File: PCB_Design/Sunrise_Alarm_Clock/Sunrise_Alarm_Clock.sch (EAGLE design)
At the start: 25 parts, among them T1 2N3904, T2 2N3904, T3 2N3904, T4 2N3904

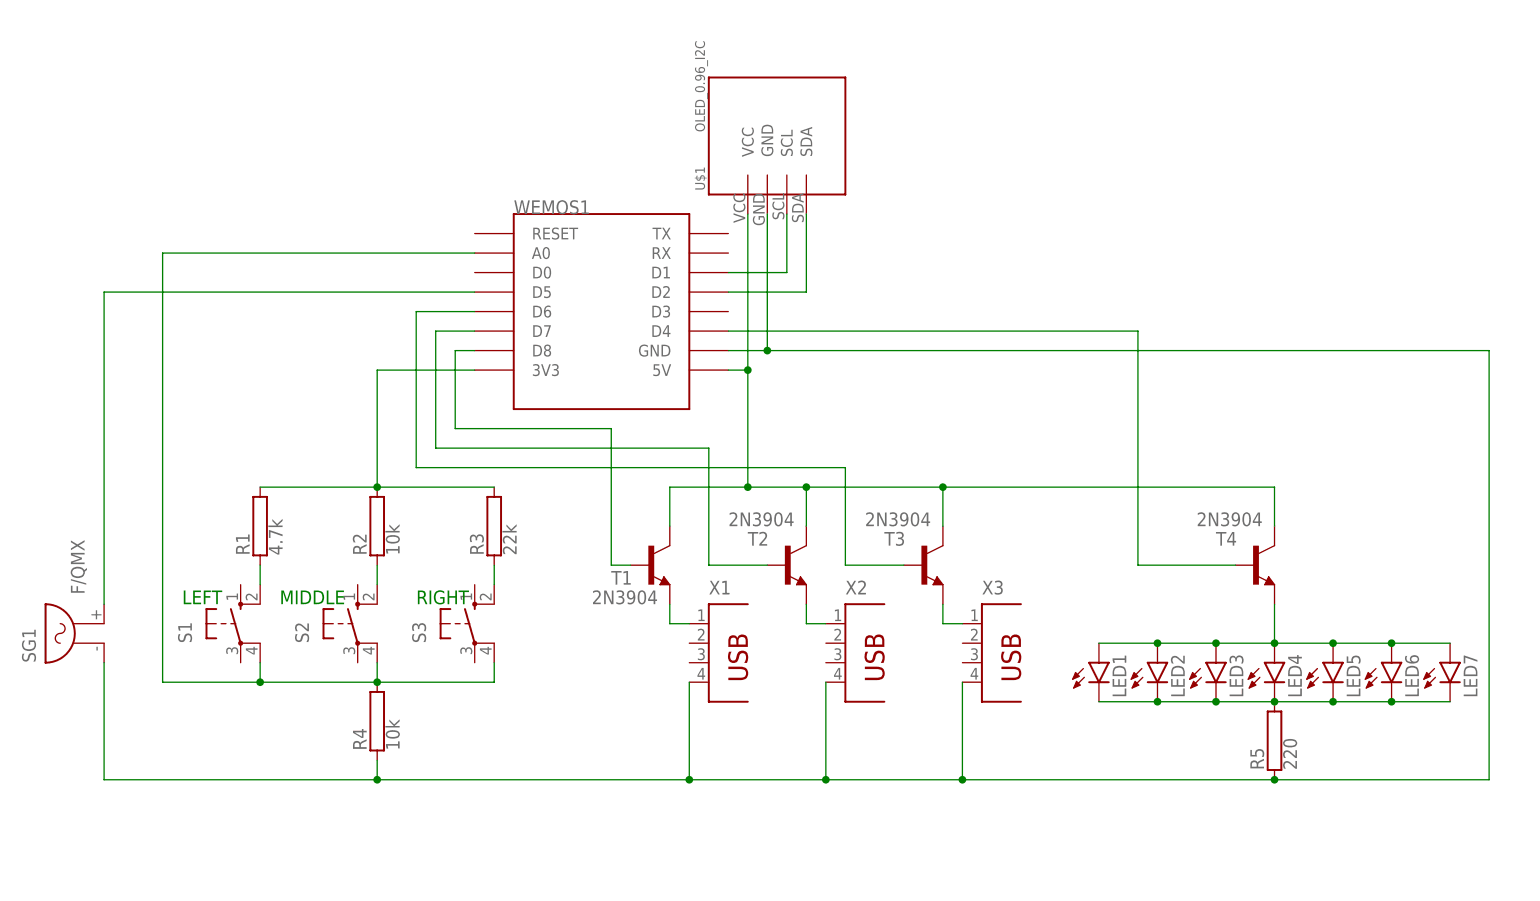
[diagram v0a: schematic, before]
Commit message: V2.1.1-alpha PCB V1.1
- Placed LEDs, USBs and D1 mini on the rear of the board
- Changed USB footprint to include shield pads
- Fixed transistors to be common-emitter
- Broke schematic into sections to make it easier to follow
- Hand-routed thicker traces
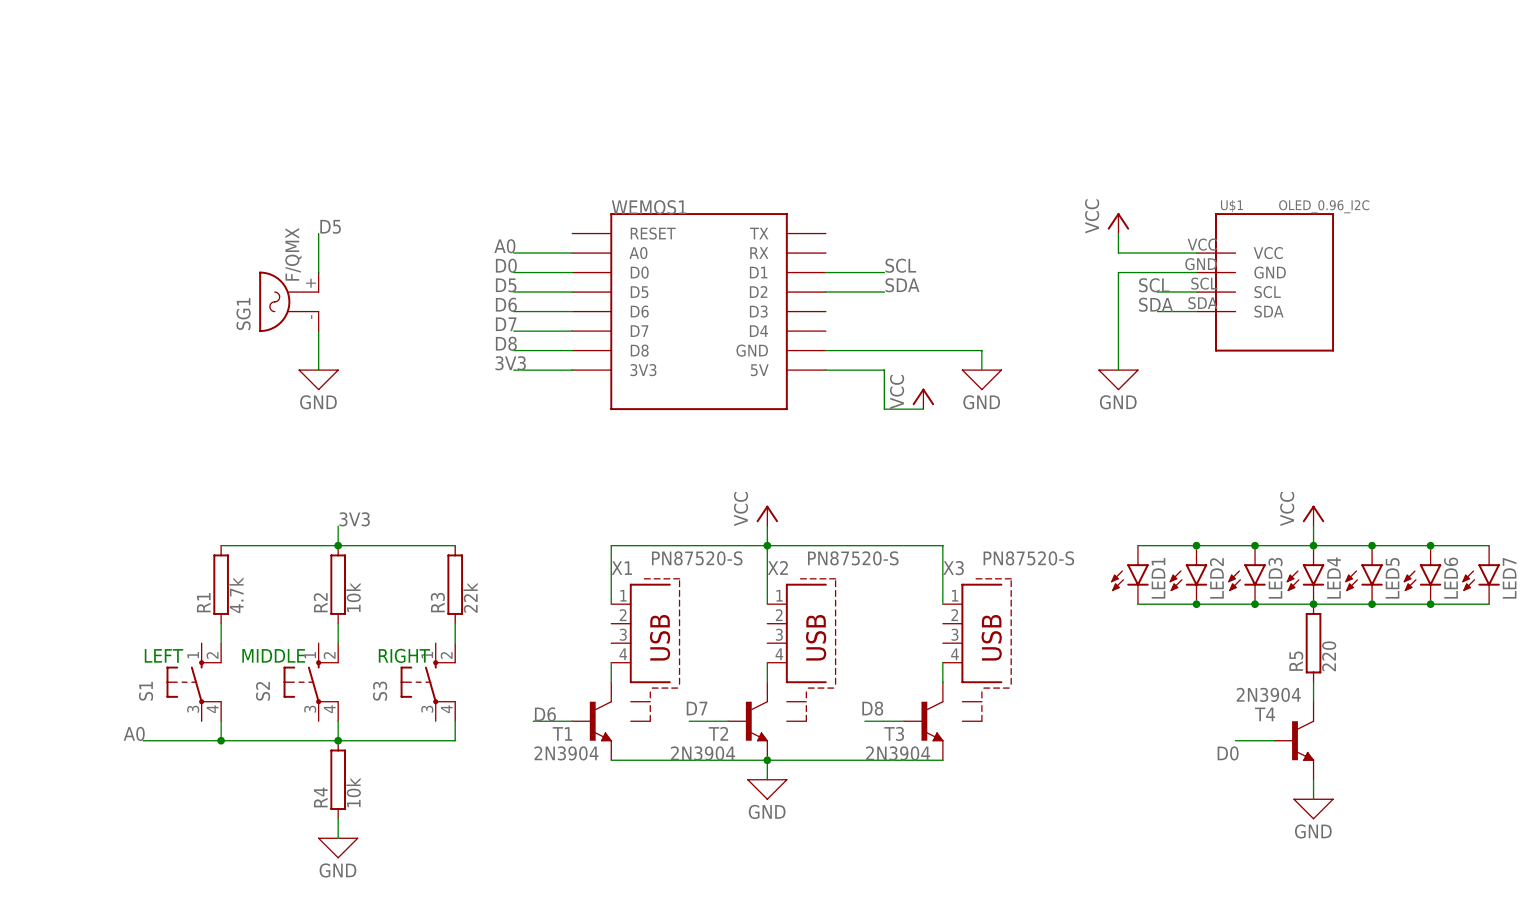
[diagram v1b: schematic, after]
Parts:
- X1, X2, X3: value (none) -> PN87520-S; device con-berg:PN87520 -> con-berg:PN87520-S
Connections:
- net N$10 renamed A0
- net N$12 renamed 3V3
- net N$15 renamed D5
- net N$17 renamed D7
- net N$3 renamed SCL
- net N$4 renamed SDA
- removed net N$13: T3.B, WEMOS1.D6
- removed net N$16: T1.B, WEMOS1.D8
- removed net N$19: LED1.A, LED2.A, LED3.A, LED4.A, LED5.A, LED6.A, LED7.A, T4.E
- removed net N$2: R4.1, R5.1, SG1.1, U$1.GND, WEMOS1.GND, X1.4, X2.4, X3.4
- removed net N$20: T4.B, WEMOS1.D4
- removed net N$7: T3.E, X3.1
- new net D0: T4.B, WEMOS1.D0
- new net D6: T1.B, WEMOS1.D6
- new net D8: T3.B, WEMOS1.D8
- new net GND: R4.1, SG1.1, T1.E, T2.E, T3.E, T4.E, U$1.GND, WEMOS1.GND
- new net N$14: R5.1, T4.C
- new net VCC: LED1.A, LED2.A, LED3.A, LED4.A, LED5.A, LED6.A, LED7.A, U$1.VCC, WEMOS1.5V, X1.1, X2.1, X3.1
- net N$1: now also X3.4; no longer T1.C, T2.C, T4.C, U$1.VCC, WEMOS1.5V
- net N$5: now also T2.C, X2.4; no longer T1.E, X1.1
- net N$6: now also T1.C, X1.4; no longer T2.E, X2.1
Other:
- moved on the sheet: LED1, LED2, LED3, LED4, LED5, LED6, LED7, R1, R2, R3, R4, R5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
